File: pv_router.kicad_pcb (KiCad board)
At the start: 4 copper layers, 75 x 69.2 mm, 49 parts, among them IC1 L6981C33DR, IC2 ATM90E26-YU-B, IC3 ESP32-C3-WROOM-02-N4, J1 Barrel_Jack_Switch_Pin3Ring, J2 AudioJack3, J3 AudioJack3, J4 Barrel_Jack_Switch_Pin3Ring, J5 UART, J6 ToSSR, Q1 BSS138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

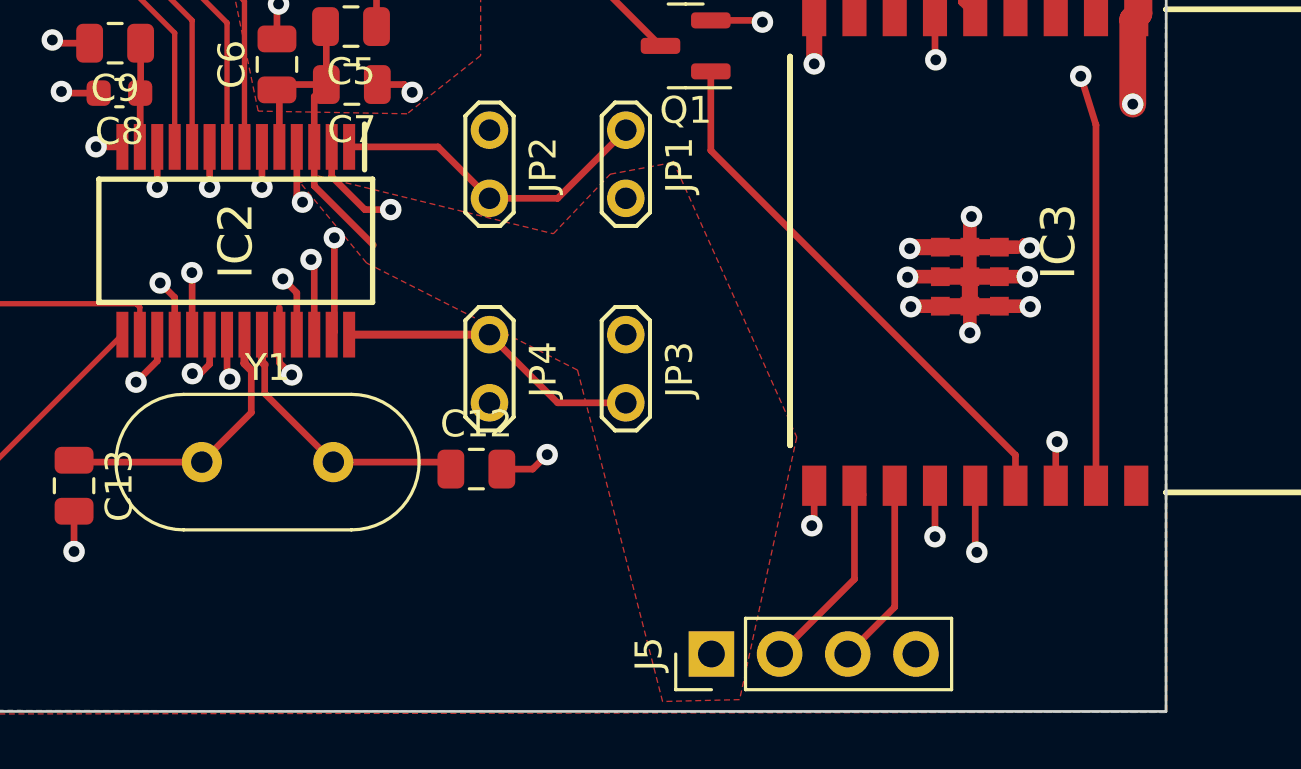
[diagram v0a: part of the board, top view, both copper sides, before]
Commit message: feat: add LED on ESP32
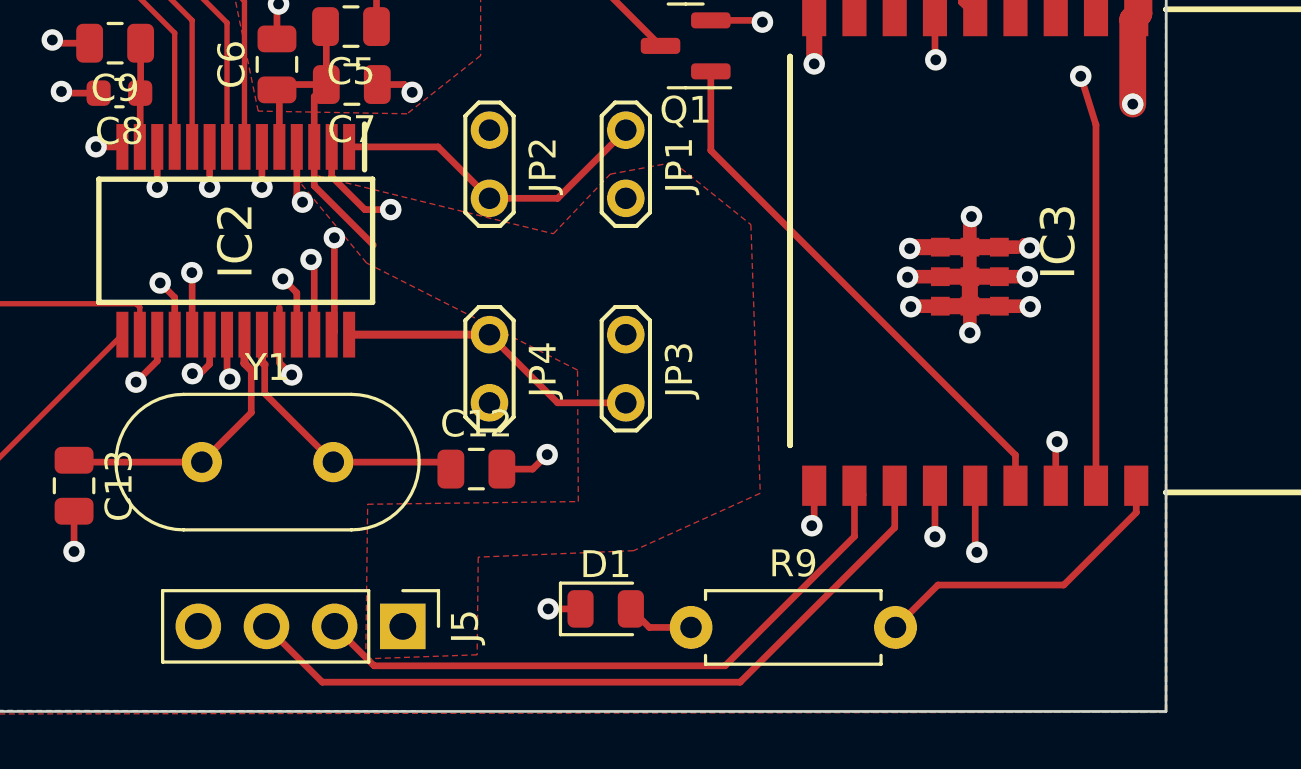
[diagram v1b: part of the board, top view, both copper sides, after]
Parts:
- added D1: LED_Small, LED_SMD:LED_0805_2012Metric, F.Cu at (179.1, 146.2)
- added R9: ?, Resistor_THT:R_Axial_DIN0207_L6.3mm_D2.5mm_P7.62mm_Horizontal, F.Cu at (182.3, 146.9)
- moved J5 11.5 mm to (171.6, 146.8), turned to -90 degrees
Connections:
- IC3 pad 18: unconnected-(IC3-IO0-Pad18) -> Net-(IC3-IO0)
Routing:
- net Net-(IC3-TXD): track 6.99 -> 28.2 mm
- net Net-(IC3-RXD): track 7.89 -> 24.3 mm
- net Net-(IC3-IO0): track 0.00 -> 11.7 mm
- net /adc/IRQ: track 39.8 -> 35.2 mm
- net /adc/WarnOut: track 45.3 -> 41.1 mm
- net Net-(D1-A): track 0.00 -> 2.53 mm
- net GND: track 78.1 -> 79.3 mm, vias 39 -> 40

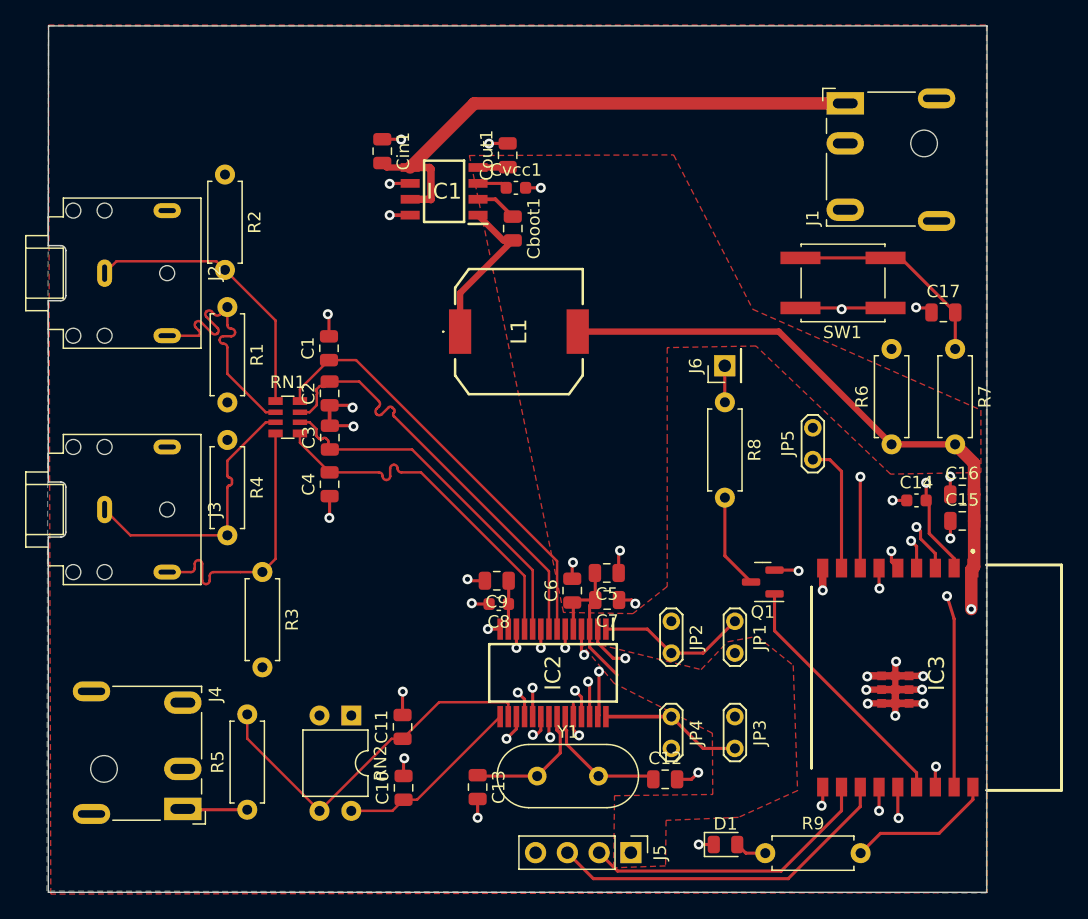
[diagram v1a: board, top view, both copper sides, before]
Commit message: text: fix silkscreen errors and add connection ref
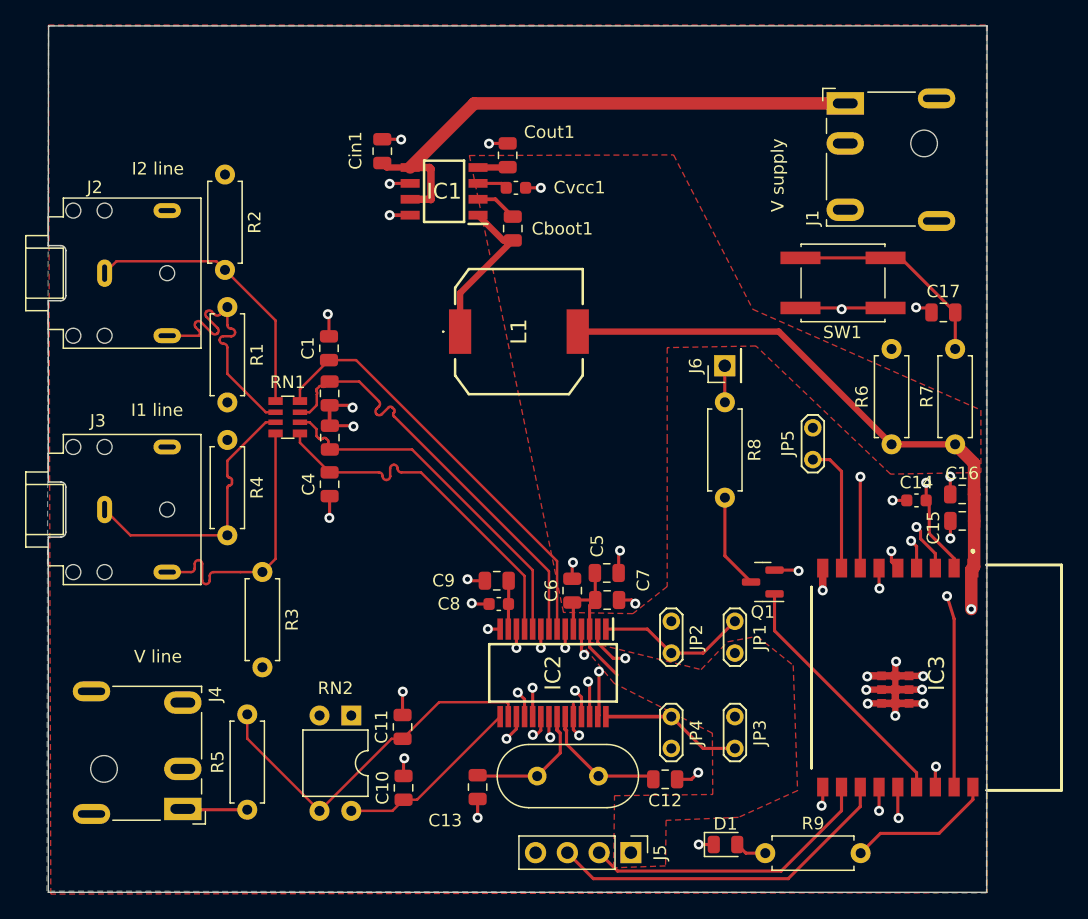
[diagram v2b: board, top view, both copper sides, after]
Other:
- board text added: "I1 line"
- board text added: "I2 line"
- board text added: "V line"
- board text added: "V supply"
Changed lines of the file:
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@@
     (property "ki_keywords" "R network parallel topology isolated")
     (attr through_hole)
-    (fp_text reference "RN2" (at 3.81 -2.33 90) (layer "F.SilkS")
+    (fp_text reference "RN2" (at -2.18 1.265 -180) (layer "F.SilkS")
         (effects (font (size 1 1) (thickness 0.15)))
     )
@@
     (property "ki_keywords" "cap capacitor")
     (attr smd)
-    (fp_text reference "C12" (at 0 -1.68) (layer "F.SilkS")
+    (fp_text reference "C12" (at -0.01 1.69) (layer "F.SilkS")
         (effects (font (size 1 1) (thickness 0.15)))
     )
@@
     (property "ki_keywords" "cap capacitor")
     (attr smd)
-    (fp_text reference "C9" (at 0 -1.68) (layer "F.SilkS")
+    (fp_text reference "C9" (at 4.25 0.01) (layer "F.SilkS")
         (effects (font (size 1 1) (thickness 0.15)))
     )
@@
     (property "ki_keywords" "cap capacitor")
     (attr smd)
-    (fp_text reference "Cout1" (at 0 -1.68 90) (layer "F.SilkS")
+    (fp_text reference "Cout1" (at 1.85 3.33 180) (layer "F.SilkS")
         (effects (font (size 1 1) (thickness 0.15)))
     )
@@
     (property "ki_keywords" "cap capacitor")
     (attr smd)
-    (fp_text reference "C2" (at 0 -1.68 90) (layer "F.SilkS")
+    (fp_text reference "C2" (at 0 -1.68 90) (layer "F.SilkS") hide
         (effects (font (size 1 1) (thickness 0.15)))
     )
@@
     (property "ki_keywords" "R res resistor")
     (attr through_hole)
-    (fp_text reference "R7" (at 3.81 -2.37 90) (layer "F.SilkS")
+    (fp_text reference "R7" (at 3.79 2.27 90) (layer "F.SilkS")
         (effects (font (size 1 1) (thickness 0.15)))
     )
@@
     (property "ki_keywords" "audio jack receptacle stereo headphones phones TRS connector")
     (attr through_hole exclude_from_pos_files)
-    (fp_text reference "J2" (at 0 -8.8 90) (layer "F.SilkS")
+    (fp_text reference "J2" (at -6.86 0.79 -180) (layer "F.SilkS")
         (effects (font (size 1 1) (thickness 0.15)))
     )
@@
     (property "ki_keywords" "cap capacitor")
     (attr smd)
-    (fp_text reference "Cvcc1" (at 0 -1.43) (layer "F.SilkS")
+    (fp_text reference "Cvcc1" (at 5.08 -0.02) (layer "F.SilkS")
         (effects (font (size 1 1) (thickness 0.15)))
     )
@@
     (property "ki_keywords" "cap capacitor")
     (attr smd)
-    (fp_text reference "C7" (at 0 -1.68) (layer "F.SilkS")
+    (fp_text reference "C7" (at -2.89 1.59 90) (layer "F.SilkS")
         (effects (font (size 1 1) (thickness 0.15)))
     )
@@
     (property "ki_keywords" "cap capacitor")
     (attr smd)
-    (fp_text reference "Cin1" (at 0 -1.68 90) (layer "F.SilkS")
+    (fp_text reference "Cin1" (at -0.05 2.14 90) (layer "F.SilkS")
         (effects (font (size 1 1) (thickness 0.15)))
     )
@@
     (property "ki_keywords" "cap capacitor")
     (attr smd)
-    (fp_text reference "C5" (at 0 -1.68) (layer "F.SilkS")
+    (fp_text reference "C5" (at 0.77 2.16 90) (layer "F.SilkS")
         (effects (font (size 1 1) (thickness 0.15)))
     )
@@
     (property "ki_keywords" "cap capacitor")
     (attr smd)
-    (fp_text reference "Cboot1" (at 0 -1.68 90) (layer "F.SilkS")
+    (fp_text reference "Cboot1" (at 0.0175 -3.96 -180) (layer "F.SilkS")
         (effects (font (size 1 1) (thickness 0.15)))
     )
@@
     (property "ki_keywords" "cap capacitor")
     (attr smd)
-    (fp_text reference "C15" (at 0 -1.68) (layer "F.SilkS")
+    (fp_text reference "C15" (at -2.31 0.54 90) (layer "F.SilkS")
         (effects (font (size 1 1) (thickness 0.15)))
     )
@@
     (property "ki_keywords" "cap capacitor")
     (attr smd)
-    (fp_text reference "C13" (at 0 -1.68 90) (layer "F.SilkS")
+    (fp_text reference "C13" (at 2.67 2.59 -180) (layer "F.SilkS")
         (effects (font (size 1 1) (thickness 0.15)))
     )
@@
     (property "ki_keywords" "cap capacitor")
     (attr smd)
-    (fp_text reference "C8" (at 0 -1.43) (layer "F.SilkS")
+    (fp_text reference "C8" (at 3.98 0.01) (layer "F.SilkS")
         (effects (font (size 1 1) (thickness 0.15)))
     )
@@
     (property "ki_keywords" "cap capacitor")
     (attr smd)
-    (fp_text reference "C3" (at 0 -1.68 90) (layer "F.SilkS")
+    (fp_text reference "C3" (at 0 -1.68 90) (layer "F.SilkS") hide
         (effects (font (size 1 1) (thickness 0.15)))
     )
@@
     (property "ki_keywords" "audio jack receptacle stereo headphones phones TRS connector")
     (attr through_hole exclude_from_pos_files)
-    (fp_text reference "J3" (at 0 -8.8 90) (layer "F.SilkS")
+    (fp_text reference "J3" (at -7.09 0.54 -180) (layer "F.SilkS")
         (effects (font (size 1 1) (thickness 0.15)))
     )
@@
     (property "ki_keywords" "quartz ceramic resonator oscillator")
     (attr through_hole)
-    (fp_text reference "Y1" (at 2.45 -3.525) (layer "F.SilkS")
+    (fp_text reference "Y1" (at 2.45 -3.525) (layer "F.SilkS") hide
         (effects (font (size 1 1) (thickness 0.15)))
     )
@@
   (gr_line (start 125.02 80.76) (end 200.02 80.76)
     (stroke (width 0.1) (type default)) (layer "Edge.Cuts"))
+  (gr_text "V supply" (at 183.88 95.64 90) (layer "F.SilkS")
+    (effects (font (size 1 1) (thickness 0.15)) (justify left bottom))
+  )
+  (gr_text "V line" (at 131.84 131.75) (layer "F.SilkS")
+    (effects (font (size 1 1) (thickness 0.15)) (justify left bottom))
+  )
+  (gr_text "I1 line" (at 131.6 112.05) (layer "F.SilkS")
+    (effects (font (size 1 1) (thickness 0.15)) (justify left bottom))
+  )
+  (gr_text "I2 line" (at 131.66 92.76) (layer "F.SilkS")
+    (effects (font (size 1 1) (thickness 0.15)) (justify left bottom))
+  )
   (segment (start 145.11 109.79) (end 147.43 107.47) (width 0.2) (layer "F.Cu") (net 1))
   (segment (start 145.11 110.74) (end 145.11 109.79) (width 0.2) (layer "F.Cu") (net 1))

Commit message: fix: capacitor value
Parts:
- C9: value 1nF -> 10nF
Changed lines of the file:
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@@
         (effects (font (size 1 1) (thickness 0.15)))
     )
-    (fp_text value "1nF" (at 0 1.68) (layer "F.Fab")
+    (fp_text value "10nF" (at 0 1.68) (layer "F.Fab")
         (effects (font (size 1 1) (thickness 0.15)))
     )

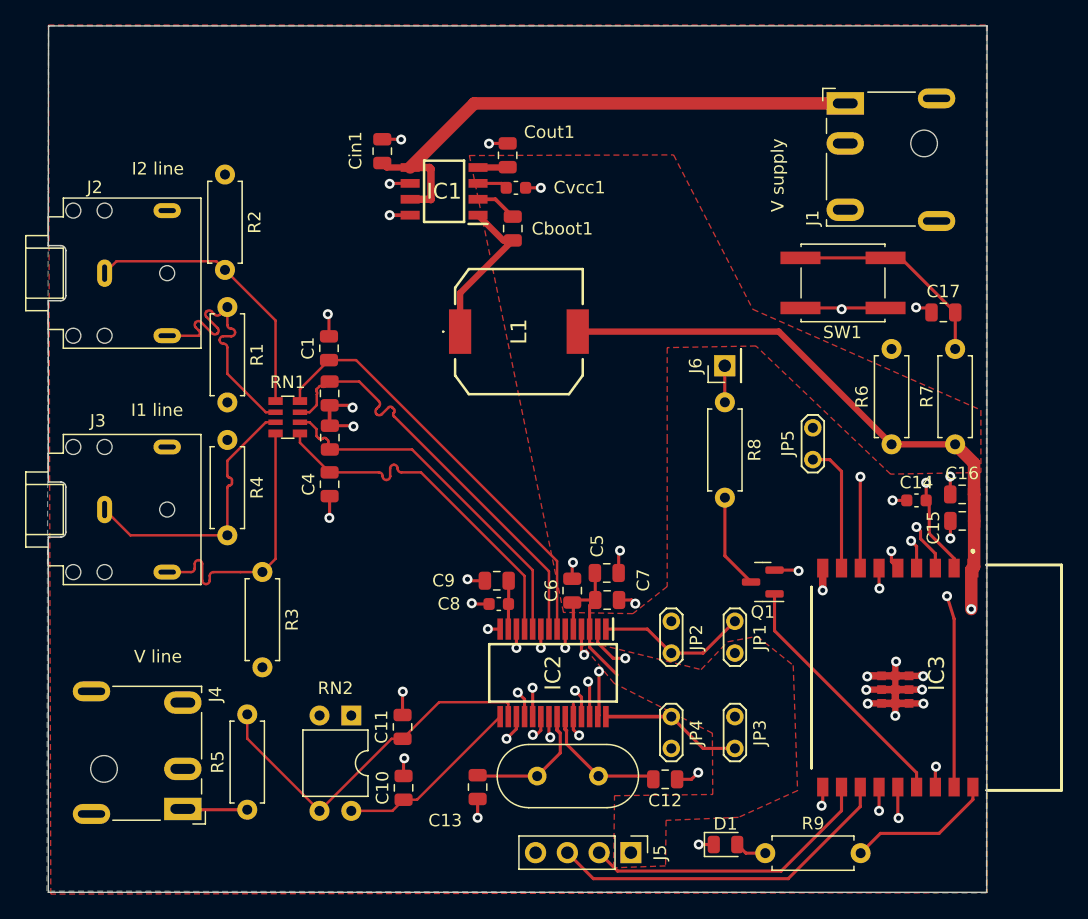
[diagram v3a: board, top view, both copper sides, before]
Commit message: pcb: define +3.3v planes in layers 1 and 3
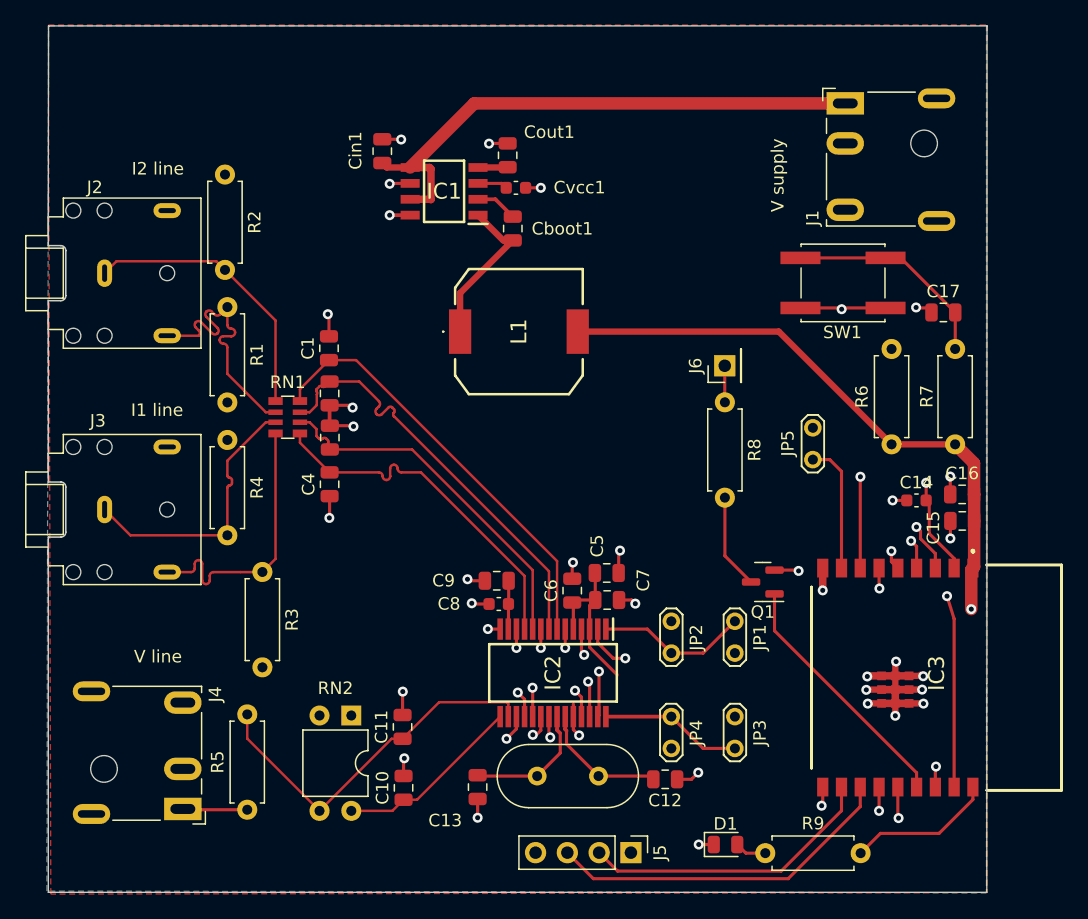
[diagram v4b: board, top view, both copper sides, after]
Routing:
- added copper zone on In2.Cu, net +3V3
- removed copper zone on F.Cu, net (none)
- removed copper zone on In2.Cu, net (none)
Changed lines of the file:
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@@
-    )
-  )
-  (zone (net 6) (net_name "+3V3") (layer "F.Cu") (hatch edge 0.5)
-    (priority 5)
-    (connect_pads yes (clearance 0.5))
-    (min_thickness 0.25) (filled_areas_thickness no)
-    (fill yes (thermal_gap 0.5) (thermal_bridge_width 0.5) (island_removal_mode 1) (island_area_min 10))
-    (polygon
-      (pts
-        (xy 184.53 131.86)
-        (xy 184.88 141.87)
-        (xy 180.16 144.01)
-        (xy 174.37 144.25)
-        (xy 174.33 147.89)
-        (xy 170.18 148.04)
-        (xy 170.25 142.28)
-        (xy 178.1 142.18)
-        (xy 178.07 137.28)
-        (xy 170.21 133.29)
-        (xy 167.735 130.294744)
-        (xy 168.385 130.0415)
-        (xy 177.17 132.2)
-        (xy 179.29 129.98)
-        (xy 181.65 129.54)
-      )
     )
   )
@@
     )
   )
-  (zone (net 6) (net_name "+3V3") (layer "F.Cu") (hatch edge 0.5)
-    (priority 5)
-    (connect_pads yes (clearance 0.5))
-    (min_thickness 0.25) (filled_areas_thickness no)
-    (fill yes (thermal_gap 0.5) (thermal_bridge_width 0.5))
-    (polygon
-      (pts
-        (xy 158.65 91.12)
-        (xy 174.97 91.07)
-        (xy 181.3 103.407396)
-        (xy 199.53 111.46)
-        (xy 199.53 116.45)
-        (xy 192.31 116.58)
-        (xy 181.55 106.34)
-        (xy 174.46 106.47)
-        (xy 174.46 113.69)
-        (xy 174.46 125.56)
-        (xy 171.72 127.73)
-        (xy 166.17 127.63)
-      )
-    )
-  )
   (zone (net 26) (net_name "/adc/RESET") (layer "F.Cu") (name "$teardrop_padvia$") (hatch edge 0.5)
     (priority 30069)
@@
     )
   )
-  (zone (net 0) (net_name "") (layer "F.Cu") (hatch edge 0.5)
+  (zone (net 6) (net_name "+3V3") (layer "F.Cu") (hatch edge 0.5)
     (priority 1)
-    (connect_pads (clearance 0.5))
+    (connect_pads yes (clearance 0.5))
     (min_thickness 0.25) (filled_areas_thickness no)
     (fill yes (thermal_gap 0.5) (thermal_bridge_width 0.5) (island_removal_mode 1) (island_area_min 10))
@@
     )
   )
-  (zone (net 0) (net_name "") (layer "In2.Cu") (hatch edge 0.5)
+  (zone (net 6) (net_name "+3V3") (layer "In2.Cu") (hatch edge 0.5)
     (priority 1)
-    (connect_pads (clearance 0.5))
+    (connect_pads yes (clearance 0.5))
     (min_thickness 0.25) (filled_areas_thickness no)
     (fill yes (thermal_gap 0.5) (thermal_bridge_width 0.5) (island_removal_mode 1) (island_area_min 10))
